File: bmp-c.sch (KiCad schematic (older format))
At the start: 66 parts, among them J1 USB_C_Receptacle_USB2.0, J2 Conn_01x10, J3 Conn_01x04, J4 JTAG-10, Q1 DMG1023DV, Q2 DMG1024UV, SW1 SW_SPST, U1 USBLC6-2SC6, U2 SN74LVC2T45YZPR, U3 SN74LVC2T45YZPR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

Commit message: Fix D1 footprint assigment
Signed-off-by: Dominik Sliwa <dominik@e-plum.pl>
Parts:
- D1: footprint Package_TO_SOT_SMD:SOT-563 -> LED_SMD:LED_0402_1005Metric
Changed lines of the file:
@@
 F 0 "D1" H 1950 2500 50  0000 C CNN
 F 1 "LED" H 1725 2500 50  0000 C CNN
-F 2 "Package_TO_SOT_SMD:SOT-563" H 1850 2450 50  0001 C CNN
+F 2 "LED_SMD:LED_0402_1005Metric" H 1850 2450 50  0001 C CNN
 F 3 "~" H 1850 2450 50  0001 C CNN
 	1    1850 2450

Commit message: Fix C7 footprint assigment
Signed-off-by: Dominik Sliwa <dominik@e-plum.pl>
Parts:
- C7: footprint Capacitor_SMD:C_0201_0603Metric -> Capacitor_SMD:C_0603_1608Metric
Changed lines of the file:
@@
 F 0 "C7" H 3250 4075 50  0000 L CNN
 F 1 "4u7" H 3250 3900 50  0000 L CNN
-F 2 "Capacitor_SMD:C_0201_0603Metric" H 3263 3850 50  0001 C CNN
+F 2 "Capacitor_SMD:C_0603_1608Metric" H 3263 3850 50  0001 C CNN
 F 3 "~" H 3225 4000 50  0001 C CNN
 	1    3225 4000

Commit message: Change STM32 footprint to include thermal vias
Signed-off-by: Dominik Sliwa <dominik@e-plum.pl>
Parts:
- U1: value USBLC6-2SC6 -> USBLC6-2P6; footprint Package_TO_SOT_SMD:SOT-23-6 -> Package_TO_SOT_SMD:SOT-666
- U6: footprint Package_DFN_QFN:QFN-48-1EP_7x7mm_P0.5mm_EP5.6x5.6mm -> Package_DFN_QFN:QFN-48-1EP_7x7mm_P0.5mm_EP5.3x5.3mm_ThermalVias
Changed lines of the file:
@@
 F 0 "U6" H 6500 5825 50  0000 C CNN
 F 1 "STM32F103CBUx" H 6675 2900 50  0000 C CNN
-F 2 "Package_DFN_QFN:QFN-48-1EP_7x7mm_P0.5mm_EP5.6x5.6mm" H 5550 2975 50  0001 R CNN
+F 2 "Package_DFN_QFN:QFN-48-1EP_7x7mm_P0.5mm_EP5.3x5.3mm_ThermalVias" H 5550 2975 50  0001 R CNN
 F 3 "http://www.st.com/st-web-ui/static/active/en/resource/technical/document/datasheet/CD00161566.pdf" H 6150 4375 50  0001 C CNN
 	1    6150 4375
@@
 P 3200 6025
 F 0 "U1" V 2850 6300 50  0000 C CNN
-F 1 "USBLC6-2SC6" V 3550 6475 50  0000 C CNN
-F 2 "Package_TO_SOT_SMD:SOT-23-6" H 2450 6425 50  0001 C CNN
+F 1 "USBLC6-2P6" V 3550 6475 50  0000 C CNN
+F 2 "Package_TO_SOT_SMD:SOT-666" H 2450 6425 50  0001 C CNN
 F 3 "http://www2.st.com/resource/en/datasheet/CD00050750.pdf" H 3400 6375 50  0001 C CNN
 	1    3200 6025

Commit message: Remove version links
Just hardwire the version

Signed-off-by: Dominik Sliwa <dominik@e-plum.pl>
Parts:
- removed JP1: v0, Jumper:SolderJumper-2_P1.3mm_Bridged_RoundedPad1.0x1.5mm, symbol Device:Jumper_NC_Small
- removed JP2: b0, Jumper:SolderJumper-2_P1.3mm_Bridged_RoundedPad1.0x1.5mm, symbol Device:Jumper_NC_Small
- removed JP3: b1, Jumper:SolderJumper-2_P1.3mm_Bridged_RoundedPad1.0x1.5mm, symbol Device:Jumper_NC_Small
- removed JP4: b2, Jumper:SolderJumper-2_P1.3mm_Open_RoundedPad1.0x1.5mm, symbol Device:Jumper_NO_Small
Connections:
- net +3V3: now also U6.40 (PB4), U6.41 (PB5), U6.42 (PB6)
- no-connect marks 12 -> 13
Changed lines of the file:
@@
-$EndComp
-$Comp
-L Device:Jumper_NC_Small JP2
-U 1 1 5D541042
-P 5250 4675
-F 0 "JP2" H 5125 4725 50  0000 C CNN
-F 1 "b0" H 5350 4725 50  0000 C CNN
-F 2 "Jumper:SolderJumper-2_P1.3mm_Bridged_RoundedPad1.0x1.5mm" H 5250 4675 50  0001 C CNN
-F 3 "~" H 5250 4675 50  0001 C CNN
-	1    5250 4675
-	1    0    0    -1
-$EndComp
-$Comp
-L Device:Jumper_NO_Small JP4
-U 1 1 5D542281
-P 5250 4875
-F 0 "JP4" H 5125 4925 50  0000 C CNN
-F 1 "b2" H 5350 4925 50  0000 C CNN
-F 2 "Jumper:SolderJumper-2_P1.3mm_Open_RoundedPad1.0x1.5mm" H 5250 4875 50  0001 C CNN
-F 3 "~" H 5250 4875 50  0001 C CNN
-	1    5250 4875
-	1    0    0    -1
 $EndComp
 $Comp
@@
 Text Notes 775  2025 0    50   ~ 0
 LEDs
-$Comp
-L Device:Jumper_NC_Small JP3
-U 1 1 5D606639
-P 5250 4775
-F 0 "JP3" H 5125 4825 50  0000 C CNN
-F 1 "b1" H 5350 4825 50  0000 C CNN
-F 2 "Jumper:SolderJumper-2_P1.3mm_Bridged_RoundedPad1.0x1.5mm" H 5250 4775 50  0001 C CNN
-F 3 "~" H 5250 4775 50  0001 C CNN
-	1    5250 4775
-	1    0    0    -1
-$EndComp
 $Comp
 L power:GND #PWR038
@@
 NoConn ~ 5450 4975
 NoConn ~ 5450 5075
-Wire Wire Line
-	5450 4675 5350 4675
-Wire Wire Line
-	5450 4775 5350 4775
-Wire Wire Line
-	5450 4875 5350 4875
-Wire Wire Line
-	5150 4675 5025 4675
 $Comp
 L power:+3V3 #PWR032
@@
 Wire Wire Line
 	5025 4675 5025 4775
-Wire Wire Line
-	5025 4875 5150 4875
-Wire Wire Line
-	5150 4775 5025 4775
 Connection ~ 5025 4775
-Wire Wire Line
-	5025 4775 5025 4875
 Wire Wire Line
 	4950 4575 5025 4575
@@
 Text Label 5050 4475 0    50   ~ 0
 TRACESWO
-$Comp
-L Device:Jumper_NC_Small JP1
-U 1 1 5D9C13F2
-P 5250 4575
-F 0 "JP1" H 5125 4625 50  0000 C CNN
-F 1 "v0" H 5350 4625 50  0000 C CNN
-F 2 "Jumper:SolderJumper-2_P1.3mm_Bridged_RoundedPad1.0x1.5mm" H 5250 4575 50  0001 C CNN
-F 3 "~" H 5250 4575 50  0001 C CNN
-	1    5250 4575
-	1    0    0    -1
-$EndComp
-Wire Wire Line
-	5450 4575 5350 4575
-Wire Wire Line
-	5150 4575 5025 4575
 Connection ~ 5025 4575
 Wire Wire Line
@@
 Wire Wire Line
 	5025 5375 4950 5375
-Wire Wire Line
-	5025 4975 5025 4875
-Connection ~ 5025 4875
 $Comp
 L power:GND #PWR026
@@
 Wire Wire Line
 	7100 5375 6750 5375
+Wire Wire Line
+	5025 4775 5025 4975
+NoConn ~ 5450 4875
+Wire Wire Line
+	5025 4575 5450 4575
+Wire Wire Line
+	5025 4675 5450 4675
+Wire Wire Line
+	5025 4775 5450 4775
 $EndSCHEMATC

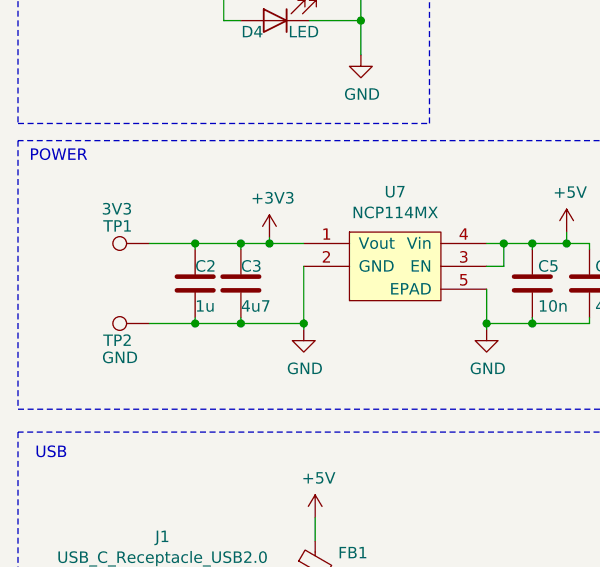
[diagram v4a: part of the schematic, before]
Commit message: Remove C2
Signed-off-by: Dominik Sliwa <dominik@e-plum.pl>
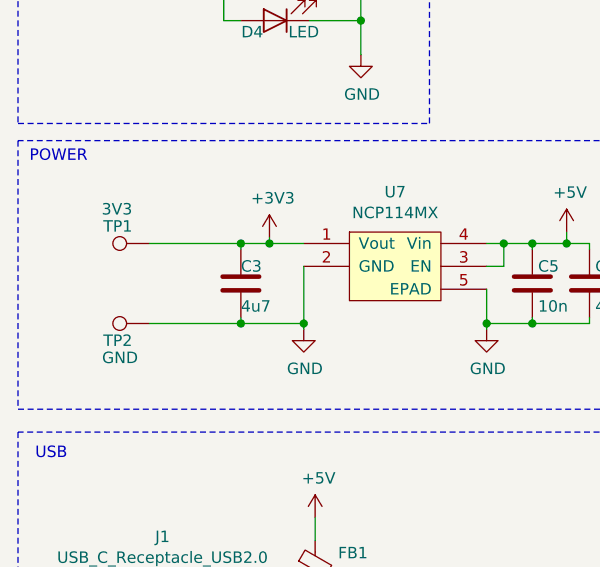
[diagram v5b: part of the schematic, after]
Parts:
- removed C2: 1u, Capacitor_SMD:C_0402_1005Metric, symbol Device:C
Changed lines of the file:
@@
 	1    0    0    -1
 $EndComp
-$Comp
-L Device:C C2
-U 1 1 5D639E69
-P 1500 4000
-F 0 "C2" H 1500 4075 50  0000 L CNN
-F 1 "1u" H 1500 3900 50  0000 L CNN
-F 2 "Capacitor_SMD:C_0402_1005Metric" H 1538 3850 50  0001 C CNN
-F 3 "~" H 1500 4000 50  0001 C CNN
-	1    1500 4000
-	1    0    0    -1
-$EndComp
-Wire Wire Line
-	1700 3825 1500 3825
-Wire Wire Line
-	1500 3825 1500 3850
 Connection ~ 1700 3825
-Wire Wire Line
-	1700 4175 1500 4175
-Wire Wire Line
-	1500 4175 1500 4150
 Connection ~ 1700 4175
 Wire Wire Line
@@
 	0    -1   -1   0
 $EndComp
-Wire Wire Line
-	1500 3825 1300 3825
-Connection ~ 1500 3825
-Wire Wire Line
-	1500 4175 1300 4175
-Connection ~ 1500 4175
 NoConn ~ 5450 3775
 NoConn ~ 5450 3875
@@
 Wire Wire Line
 	5025 4775 5450 4775
+Wire Wire Line
+	1300 4175 1700 4175
+Wire Wire Line
+	1300 3825 1700 3825
 $EndSCHEMATC
